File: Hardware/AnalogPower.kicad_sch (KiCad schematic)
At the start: 0 parts

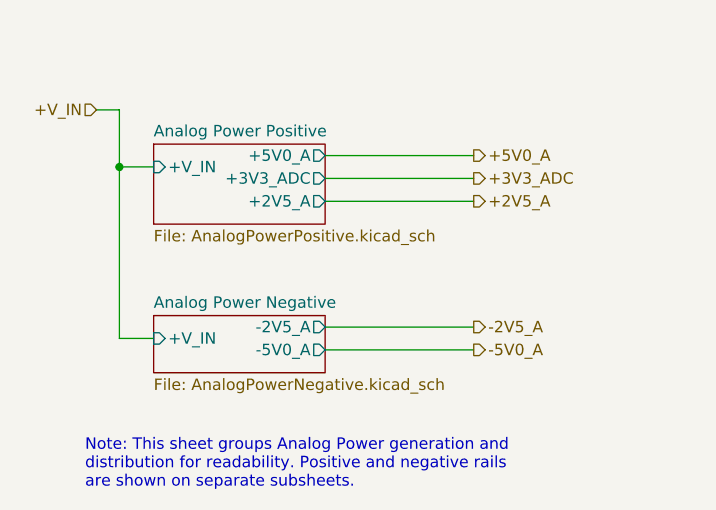
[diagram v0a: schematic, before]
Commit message: fix: #134
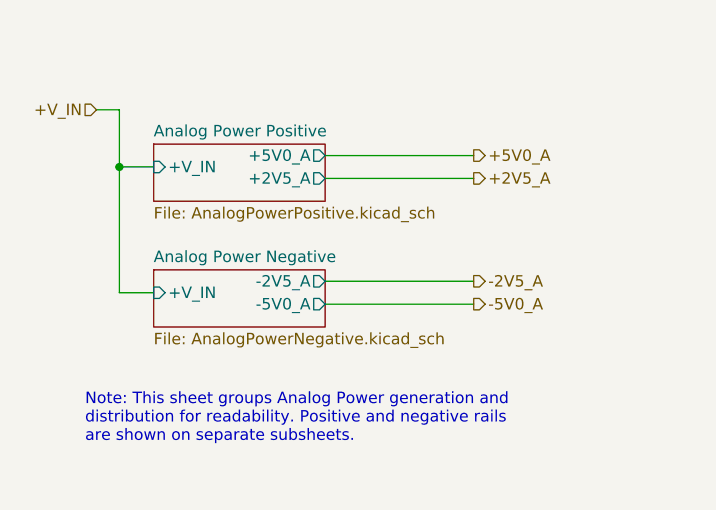
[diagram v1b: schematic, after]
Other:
- sheet Analog Power Positive ports: added none; removed +3V3_ADC
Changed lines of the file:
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@@
 		(title "Analog Power")
 		(date "2026-04-11")
-		(rev "1.0")
+		(rev "0.1")
 		(company "RG")
 		(comment 2 "Schematic Diagram")
@@
 	(text "Note: This sheet groups Analog Power generation and \ndistribution for readability. Positive and negative rails \nare shown on separate subsheets."
 		(exclude_from_sim no)
-		(at 45.72 82.55 0)
+		(at 45.72 77.47 0)
 		(effects
 			(font
@@
 	(wire
 		(pts
-			(xy 88.9 69.85) (xy 72.39 69.85)
-		)
-		(stroke
-			(width 0)
-			(type default)
-		)
-	)
-	(wire
-		(pts
-			(xy 72.39 67.31) (xy 88.9 67.31)
+			(xy 72.39 64.77) (xy 88.9 64.77)
+		)
+		(stroke
+			(width 0)
+			(type default)
+		)
+	)
+	(wire
+		(pts
+			(xy 72.39 62.23) (xy 88.9 62.23)
 		)
 		(stroke
@@
 	(wire
 		(pts
-			(xy 49.53 49.53) (xy 49.53 68.58)
-		)
-		(stroke
-			(width 0)
-			(type default)
-		)
-	)
-	(wire
-		(pts
-			(xy 72.39 53.34) (xy 88.9 53.34)
-		)
-		(stroke
-			(width 0)
-			(type default)
-		)
-	)
-	(wire
-		(pts
-			(xy 49.53 68.58) (xy 53.34 68.58)
+			(xy 49.53 49.53) (xy 49.53 63.5)
 		)
 		(stroke
@@
 	(wire
 		(pts
+			(xy 49.53 63.5) (xy 53.34 63.5)
+		)
+		(stroke
+			(width 0)
+			(type default)
+		)
+	)
+	(wire
+		(pts
 			(xy 49.53 43.18) (xy 49.53 49.53)
 		)
@@
 	(hierarchical_label "-5V0_A"
 		(shape output)
-		(at 88.9 69.85 0)
-		(effects
-			(font
-				(size 1.27 1.27)
-			)
-			(justify left)
-		)
-	)
-	(hierarchical_label "+3V3_ADC"
+		(at 88.9 64.77 0)
+		(effects
+			(font
+				(size 1.27 1.27)
+			)
+			(justify left)
+		)
+	)
+	(hierarchical_label "+5V0_A"
+		(shape output)
+		(at 88.9 48.26 0)
+		(effects
+			(font
+				(size 1.27 1.27)
+			)
+			(justify left)
+		)
+	)
+	(hierarchical_label "+2V5_A"
 		(shape output)
 		(at 88.9 50.8 0)
-		(effects
-			(font
-				(size 1.27 1.27)
-			)
-			(justify left)
-		)
-	)
-	(hierarchical_label "+5V0_A"
-		(shape output)
-		(at 88.9 48.26 0)
-		(effects
-			(font
-				(size 1.27 1.27)
-			)
-			(justify left)
-		)
-	)
-	(hierarchical_label "+2V5_A"
-		(shape output)
-		(at 88.9 53.34 0)
 		(effects
 			(font
@@
 	(hierarchical_label "-2V5_A"
 		(shape output)
-		(at 88.9 67.31 0)
+		(at 88.9 62.23 0)
 		(effects
 			(font
@@
 	)
 	(sheet
-		(at 53.34 66.04)
+		(at 53.34 60.96)
 		(size 19.05 6.35)
 		(exclude_from_sim no)
@@
 		)
 		(property "Sheetname" "Analog Power Negative"
-			(at 53.34 65.3284 0)
+			(at 53.34 60.2484 0)
 			(show_name no)
 			(do_not_autoplace no)
@@
 		)
 		(property "Sheetfile" "AnalogPowerNegative.kicad_sch"
-			(at 53.34 72.9746 0)
+			(at 53.34 67.8946 0)
 			(show_name no)
 			(do_not_autoplace no)
@@
 		)
 		(pin "+V_IN" input
-			(at 53.34 68.58 180)
+			(at 53.34 63.5 180)
 			(effects
 				(font
@@
 		)
 		(pin "-2V5_A" output
-			(at 72.39 67.31 0)
+			(at 72.39 62.23 0)
 			(effects
 				(font
@@
 		)
 		(pin "-5V0_A" output
-			(at 72.39 69.85 0)
+			(at 72.39 64.77 0)
 			(effects
 				(font
@@
 	(sheet
 		(at 53.34 46.99)
-		(size 19.05 8.89)
+		(size 19.05 6.35)
 		(exclude_from_sim no)
 		(in_bom yes)
@@
 		)
 		(property "Sheetfile" "AnalogPowerPositive.kicad_sch"
-			(at 53.34 56.4646 0)
+			(at 53.34 53.9246 0)
 			(show_name no)
 			(do_not_autoplace no)
@@
 		)
 		(pin "+2V5_A" output
-			(at 72.39 53.34 0)
+			(at 72.39 50.8 0)
 			(effects
 				(font
@@
 			(effects
 				(font
-					(size 1.27 1.27)
-				)
-				(justify right)
-			)
-		)
-		(pin "+3V3_ADC" output
-			(at 72.39 50.8 0)
-			(effects
-				(font

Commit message: fix: #170, fix: #144, fix: #132
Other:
- sheet Analog Power Negative ports: added none; removed -2V5_A
- sheet Analog Power Positive ports: added none; removed +2V5_A
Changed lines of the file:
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@@
-	(wire
-		(pts
-			(xy 72.39 62.23) (xy 88.9 62.23)
-		)
-		(stroke
-			(width 0)
-			(type default)
-		)
-	)
 	(wire
 		(pts
@@
 	(wire
 		(pts
-			(xy 72.39 50.8) (xy 88.9 50.8)
-		)
-		(stroke
-			(width 0)
-			(type default)
-		)
-	)
-	(wire
-		(pts
 			(xy 49.53 63.5) (xy 53.34 63.5)
 		)
@@
 		)
 	)
-	(hierarchical_label "-5V0_A"
+	(hierarchical_label "-3V3_A"
 		(shape output)
-		(at 88.9 64.77 0)
+		(at 97.79 58.42 0)
 		(effects
 			(font
@@
 		)
 	)
-	(hierarchical_label "+5V0_A"
+	(hierarchical_label "+3V3_A"
 		(shape output)
-		(at 88.9 48.26 0)
-		(effects
-			(font
-				(size 1.27 1.27)
-			)
-			(justify left)
-		)
-	)
-	(hierarchical_label "+2V5_A"
-		(shape output)
-		(at 88.9 50.8 0)
+		(at 90.17 34.29 0)
 		(effects
 			(font
@@
 			)
 			(justify right)
-		)
-	)
-	(hierarchical_label "-2V5_A"
-		(shape output)
-		(at 88.9 62.23 0)
-		(effects
-			(font
-				(size 1.27 1.27)
-			)
-			(justify left)
 		)
 	)
@@
 			)
 		)
-		(pin "-2V5_A" output
-			(at 72.39 62.23 0)
-			(effects
-				(font
-					(size 1.27 1.27)
-				)
-				(justify right)
-			)
-		)
 		(pin "-5V0_A" output
 			(at 72.39 64.77 0)
@@
 			(project "GammaSpectrometer"
 				(path "/d6192878-4721-4ef4-99ff-dbbad0502886/b16128e5-6398-4e08-86d4-8842ad98ebb1"
-					(page "8")
+					(page "15")
 				)
 			)
@@
 			)
 		)
-		(pin "+2V5_A" output
-			(at 72.39 50.8 0)
-			(effects
-				(font
-					(size 1.27 1.27)
-				)
-				(justify right)
-			)
-		)
 		(pin "+5V0_A" output
 			(at 72.39 48.26 0)
@@
 			(project "GammaSpectrometer"
 				(path "/d6192878-4721-4ef4-99ff-dbbad0502886/b16128e5-6398-4e08-86d4-8842ad98ebb1"
-					(page "10")
-				)
-			)
+					(page "16")
+				)
+			)
